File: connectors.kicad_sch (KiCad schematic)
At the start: 4 parts, among them J1 Conn_01x04_Pin, J2 Conn_01x04_Pin, J3 Conn_01x09_Pin, J4 Conn_02x03_Odd_Even

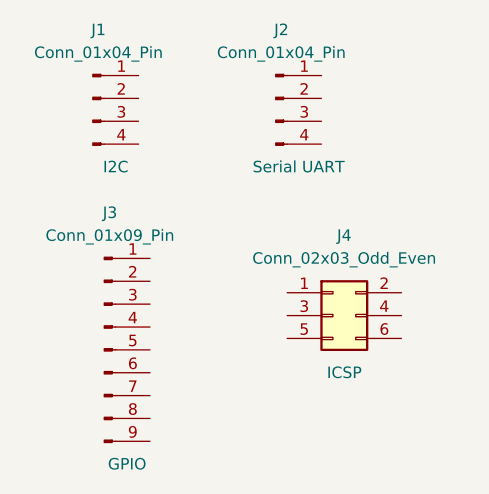
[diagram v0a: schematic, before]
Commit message: Complete wiring in the second sheet
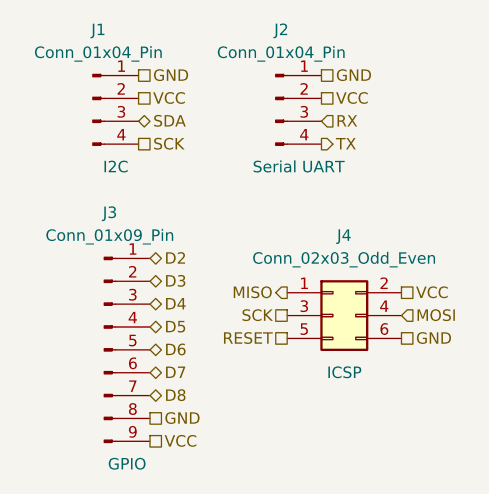
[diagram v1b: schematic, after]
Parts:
- J1, J2: footprint (none) -> Connector_PinHeader_2.54mm:PinHeader_1x04_P2.54mm_Vertical
- J3: footprint (none) -> Connector_PinHeader_2.54mm:PinHeader_1x09_P2.54mm_Vertical
- J4: footprint (none) -> Connector_PinHeader_2.54mm:PinHeader_2x03_P2.54mm_Vertical
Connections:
- net D2: now reaches J3.1 (Pin_1)
- net D3: now reaches J3.2 (Pin_2)
- net D4: now reaches J3.3 (Pin_3)
- net D5: now reaches J3.4 (Pin_4)
- net D6: now reaches J3.5 (Pin_5)
- net D7: now reaches J3.6 (Pin_6)
- net D8: now reaches J3.7 (Pin_7)
- net GND: now reaches J3.8 (Pin_8)
- net GND: now also J1.1 (Pin_1), J2.1 (Pin_1), J4.6 (Pin_6)
- net VCC: now reaches J3.9 (Pin_9)
- net VCC: now also J1.2 (Pin_2), J2.2 (Pin_2), J4.2 (Pin_2)
- net MISO: now reaches J4.1 (Pin_1)
- net SCK: now reaches J4.3 (Pin_3)
- net SCK: now also J1.4 (Pin_4)
- net MOSI: now reaches J4.4 (Pin_4)
- net RESET: now reaches J4.5 (Pin_5)
- net SDA: now reaches J1.3 (Pin_3)
- net RX: now reaches J2.3 (Pin_3)
- net TX: now reaches J2.4 (Pin_4)
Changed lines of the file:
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@@
 (kicad_sch (version 20230121) (generator eeschema)
   (paper "A4")
+  (hierarchical_label "D2" (shape bidirectional) (at 93.98 86.36 0) (fields_autoplaced)
+    (effects (font (size 1.27 1.27)) (justify left))
+  )
+  (hierarchical_label "VCC" (shape passive) (at 121.92 90.17 0) (fields_autoplaced)
+    (effects (font (size 1.27 1.27)) (justify left))
+  )
+  (hierarchical_label "D5" (shape bidirectional) (at 93.98 93.98 0) (fields_autoplaced)
+    (effects (font (size 1.27 1.27)) (justify left))
+  )
+  (hierarchical_label "GND" (shape passive) (at 113.03 66.04 0) (fields_autoplaced)
+    (effects (font (size 1.27 1.27)) (justify left))
+  )
+  (hierarchical_label "GND" (shape passive) (at 92.71 66.04 0) (fields_autoplaced)
+    (effects (font (size 1.27 1.27)) (justify left))
+  )
+  (hierarchical_label "D8" (shape bidirectional) (at 93.98 101.6 0) (fields_autoplaced)
+    (effects (font (size 1.27 1.27)) (justify left))
+  )
+  (hierarchical_label "SDA" (shape bidirectional) (at 92.71 71.12 0) (fields_autoplaced)
+    (effects (font (size 1.27 1.27)) (justify left))
+  )
+  (hierarchical_label "SCK" (shape passive) (at 92.71 73.66 0) (fields_autoplaced)
+    (effects (font (size 1.27 1.27)) (justify left))
+  )
+  (hierarchical_label "D6" (shape bidirectional) (at 93.98 96.52 0) (fields_autoplaced)
+    (effects (font (size 1.27 1.27)) (justify left))
+  )
+  (hierarchical_label "MISO" (shape output) (at 109.22 90.17 180) (fields_autoplaced)
+    (effects (font (size 1.27 1.27)) (justify right))
+  )
+  (hierarchical_label "VCC" (shape passive) (at 113.03 68.58 0) (fields_autoplaced)
+    (effects (font (size 1.27 1.27)) (justify left))
+  )
+  (hierarchical_label "VCC" (shape passive) (at 92.71 68.58 0) (fields_autoplaced)
+    (effects (font (size 1.27 1.27)) (justify left))
+  )
+  (hierarchical_label "VCC" (shape passive) (at 93.98 106.68 0) (fields_autoplaced)
+    (effects (font (size 1.27 1.27)) (justify left))
+  )
+  (hierarchical_label "D4" (shape bidirectional) (at 93.98 91.44 0) (fields_autoplaced)
+    (effects (font (size 1.27 1.27)) (justify left))
+  )
+  (hierarchical_label "SCK" (shape passive) (at 109.22 92.71 180) (fields_autoplaced)
+    (effects (font (size 1.27 1.27)) (justify right))
+  )
+  (hierarchical_label "TX" (shape output) (at 113.03 73.66 0) (fields_autoplaced)
+    (effects (font (size 1.27 1.27)) (justify left))
+  )
+  (hierarchical_label "GND" (shape passive) (at 93.98 104.14 0) (fields_autoplaced)
+    (effects (font (size 1.27 1.27)) (justify left))
+  )
+  (hierarchical_label "D7" (shape bidirectional) (at 93.98 99.06 0) (fields_autoplaced)
+    (effects (font (size 1.27 1.27)) (justify left))
+  )
+  (hierarchical_label "RX" (shape input) (at 113.03 71.12 0) (fields_autoplaced)
+    (effects (font (size 1.27 1.27)) (justify left))
+  )
+  (hierarchical_label "MOSI" (shape input) (at 121.92 92.71 0) (fields_autoplaced)
+    (effects (font (size 1.27 1.27)) (justify left))
+  )
+  (hierarchical_label "RESET" (shape passive) (at 109.22 95.25 180) (fields_autoplaced)
+    (effects (font (size 1.27 1.27)) (justify right))
+  )
+  (hierarchical_label "D3" (shape bidirectional) (at 93.98 88.9 0) (fields_autoplaced)
+    (effects (font (size 1.27 1.27)) (justify left))
+  )
+  (hierarchical_label "GND" (shape passive) (at 121.92 95.25 0) (fields_autoplaced)
+    (effects (font (size 1.27 1.27)) (justify left))
+  )
   (symbol (lib_id "Connector:Conn_01x09_Pin") (at 88.9 96.52 0) (unit 1)
     (in_bom yes) (on_board yes) (dnp no)
@@
       (effects (font (size 1.27 1.27)))
     )
-    (property "Footprint" "" (at 88.9 96.52 0)
+    (property "Footprint" "Connector_PinHeader_2.54mm:PinHeader_1x09_P2.54mm_Vertical" (at 88.9 96.52 0)
       (effects (font (size 1.27 1.27)) hide)
     )
@@
       (effects (font (size 1.27 1.27)))
     )
-    (property "Footprint" "" (at 114.3 92.71 0)
+    (property "Footprint" "Connector_PinHeader_2.54mm:PinHeader_2x03_P2.54mm_Vertical" (at 114.3 92.71 0)
       (effects (font (size 1.27 1.27)) hide)
     )
@@
       (effects (font (size 1.27 1.27)))
     )
-    (property "Footprint" "" (at 87.63 68.58 0)
+    (property "Footprint" "Connector_PinHeader_2.54mm:PinHeader_1x04_P2.54mm_Vertical" (at 87.63 68.58 0)
       (effects (font (size 1.27 1.27)) hide)
     )
@@
       (effects (font (size 1.27 1.27)))
     )
-    (property "Footprint" "" (at 107.95 68.58 0)
+    (property "Footprint" "Connector_PinHeader_2.54mm:PinHeader_1x04_P2.54mm_Vertical" (at 107.95 68.58 0)
       (effects (font (size 1.27 1.27)) hide)
     )

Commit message: Connections established
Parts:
- renumbered J3 to J2, J2 to J3
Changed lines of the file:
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@@
   (symbol (lib_id "Connector:Conn_01x09_Pin") (at 88.9 96.52 0) (unit 1)
     (in_bom yes) (on_board yes) (dnp no)
-    (property "Reference" "J3" (at 89.535 81.28 0)
+    (property "Reference" "J2" (at 89.535 81.28 0)
       (effects (font (size 1.27 1.27)))
     )
@@
       (project "MCUdatalogger_V1"
         (path "/b93563e1-8fe5-4271-839f-45f8ce901c22/0cf192c1-f9bc-4a5d-87a5-6c04f2d03566"
-          (reference "J3") (unit 1)
+          (reference "J2") (unit 1)
         )
       )
@@
   (symbol (lib_id "Connector:Conn_01x04_Pin") (at 107.95 68.58 0) (unit 1)
     (in_bom yes) (on_board yes) (dnp no)
-    (property "Reference" "J2" (at 108.585 60.96 0)
+    (property "Reference" "J3" (at 108.585 60.96 0)
       (effects (font (size 1.27 1.27)))
     )
@@
       (project "MCUdatalogger_V1"
         (path "/b93563e1-8fe5-4271-839f-45f8ce901c22/0cf192c1-f9bc-4a5d-87a5-6c04f2d03566"
-          (reference "J2") (unit 1)
+          (reference "J3") (unit 1)
         )
       )
